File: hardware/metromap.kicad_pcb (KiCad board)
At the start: 4 copper layers, 100 x 100 mm, 138 parts, among them J1 USB_C_Receptacle_USB2.0_16P, U1 AZ1117-3.3, U2 ESP32-C6-MINI-1-H4, U3 SN74LVC1G125DBV

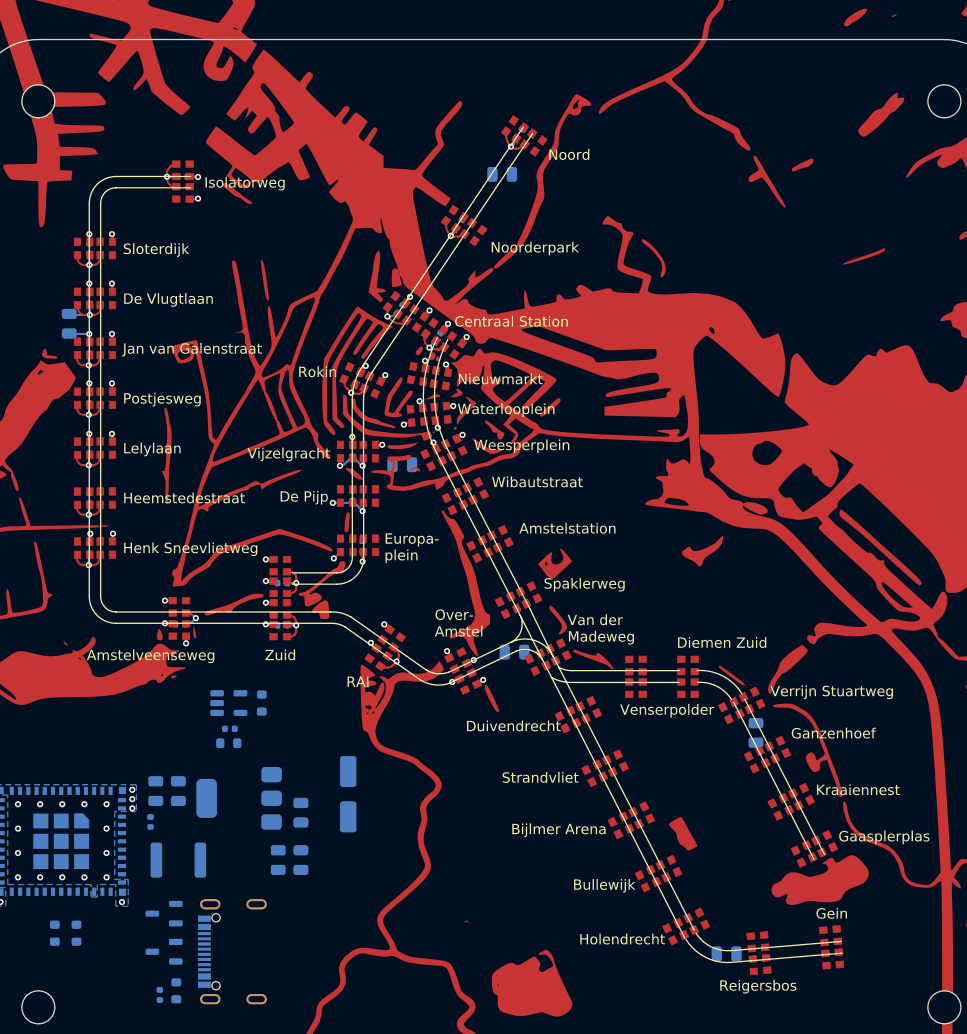
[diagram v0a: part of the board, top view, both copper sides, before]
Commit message: Routed half of leds
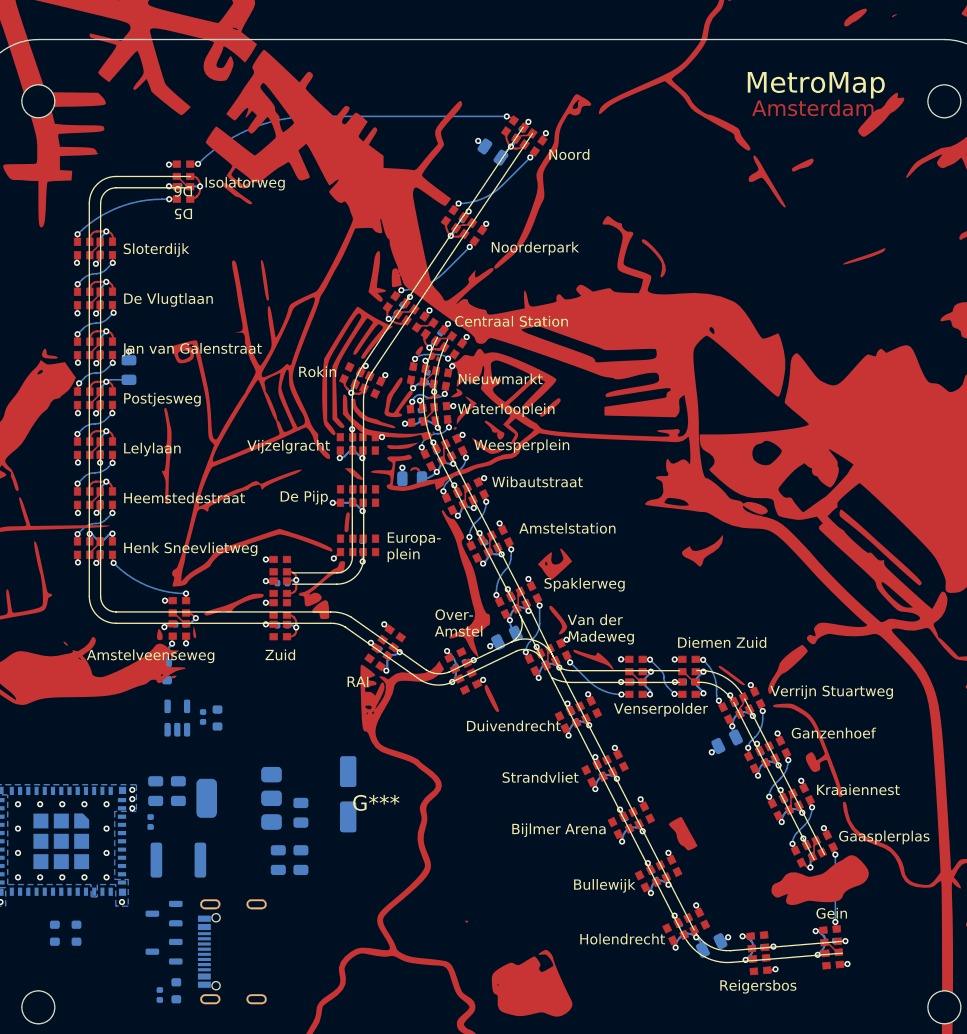
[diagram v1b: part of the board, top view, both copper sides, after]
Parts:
- removed the D3 at (82.2, 41.7)
- removed the D4 at (82.2, 43.9)
- added C35: 100n, Capacitor_SMD:C_0402_1005Metric, B.Cu at (107.1, 69.4)
- added C36: 100n, Capacitor_SMD:C_0402_1005Metric, B.Cu at (109.2, 73.6)
- added C37: 100n, Capacitor_SMD:C_0402_1005Metric, B.Cu at (114.4, 83.7)
- added C38: 100n, Capacitor_SMD:C_0402_1005Metric, B.Cu at (120.2, 94.8)
- added C39: 100n, Capacitor_SMD:C_0402_1005Metric, B.Cu at (122.8, 100.0)
- added C40: 100n, Capacitor_SMD:C_0402_1005Metric, B.Cu at (105.4, 65.5)
- added C41: 100n, Capacitor_SMD:C_0402_1005Metric, B.Cu at (111.8, 78.3)
- added C42: 100n, Capacitor_SMD:C_0402_1005Metric, B.Cu at (101.7, 88.5)
- added C43: 100n, Capacitor_SMD:C_0402_1005Metric, B.Cu at (128.0, 110.2)
- added C44: 100n, Capacitor_SMD:C_0402_1005Metric, B.Cu at (125.4, 105.1)
- added C45: 100n, Capacitor_SMD:C_0402_1005Metric, B.Cu at (105.9, 61.8)
- added C46: 100n, Capacitor_SMD:C_0402_1005Metric, B.Cu at (109.2, 89.7)
- added C47: 100n, Capacitor_SMD:C_0402_1005Metric, B.Cu at (117.2, 89.2)
- added C48: 100n, Capacitor_SMD:C_0402_1005Metric, B.Cu at (130.7, 115.4)
- added C49: 100n, Capacitor_SMD:C_0402_1005Metric, B.Cu at (126.3, 91.4)
- added C50: 100n, Capacitor_SMD:C_0402_1005Metric, B.Cu at (131.4, 91.4)
- added C51: 100n, Capacitor_SMD:C_0402_1005Metric, B.Cu at (136.1, 93.9)
- added C52: 100n, Capacitor_SMD:C_0402_1005Metric, B.Cu at (138.6, 98.7)
- added C53: 100n, Capacitor_SMD:C_0402_1005Metric, B.Cu at (140.9, 103.3)
- added C54: 100n, Capacitor_SMD:C_0402_1005Metric, B.Cu at (143.1, 107.8)
- added C55: 100n, Capacitor_SMD:C_0402_1005Metric, B.Cu at (145.1, 116.6)
- added C56: 100n, Capacitor_SMD:C_0402_1005Metric, B.Cu at (138.1, 117.2)
- added D5: SK6812-EC20, metro-tracker:RGB_LED_2020, F.Cu at (82.3, 43.9)
- added D6: SK6812-EC20, metro-tracker:RGB_LED_2020, F.Cu at (82.3, 41.7)
- moved D42 29.2 mm to (74.8, 49.3), turned to -90 degrees
- moved D10 29.2 mm to (72.6, 78.4), turned to -90 degrees
- moved D9 29.2 mm to (74.8, 78.4), turned to -90 degrees
- moved D43 29.2 mm to (72.6, 49.3), turned to -90 degrees
- moved C26 29.1 mm to (74.2, 49.3), turned to -90 degrees
- moved C18 29.1 mm to (74.2, 78.4), turned to -90 degrees
- moved D38 19.5 mm to (74.8, 54.1), turned to -90 degrees
- moved D21 19.5 mm to (72.6, 73.5), turned to -90 degrees
- moved D20 19.5 mm to (74.8, 73.5), turned to -90 degrees
- moved D39 19.5 mm to (72.6, 54.1), turned to -90 degrees
- moved C27 19.4 mm to (74.2, 54.1), turned to -90 degrees
- moved C19 19.4 mm to (74.2, 73.5), turned to -90 degrees
- moved D73 9.96 mm to (74.8, 59.0), turned to -90 degrees
- moved D26 9.95 mm to (72.6, 68.7), turned to -90 degrees
- moved D25 9.94 mm to (74.8, 68.7), turned to -90 degrees
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- renumbered C34 to C1, C26 to C10, C28 to C11, C29 to C12, C30 to C13, C31 to C14, C25 to C15, C19 to C16, C20 to C17, C21 to C18, C22 to C19, C33 to C2, C23 to C20, C24 to C21, C13 to C22, C14 to C23, C15 to C24, C16 to C25, C17 to C26, C18 to C27, C12 to C28, C11 to C29, C32 to C3, C10 to C30, C9 to C31, C8 to C32, C7 to C33, C6 to C34, C5 to C4, C4 to C5, C3 to C6, C1 to C7, C2 to C8, C27 to C9, D83 to D1, D8 to D10, D9 to D11, D31 to D12, D32 to D13, D79 to D14, D80 to D15, D81 to D16, D82 to D17, D77 to D18, D78 to D19, D84 to D2, D10 to D20, D11 to D21, D12 to D22, D13 to D23, D14 to D24, D15 to D25, D16 to D26, D17 to D27, D18 to D28, D19 to D29, D1 to D3, D20 to D30, D21 to D31, D22 to D32, D23 to D33, D24 to D34, D25 to D35, D26 to D36, D33 to D37, D34 to D38, D35 to D39, D2 to D4, D36 to D40, D37 to D41, D38 to D42, D39 to D43, D40 to D44, D41 to D45, D42 to D46, D43 to D47, D44 to D48, D45 to D49, D46 to D50, D47 to D51, D48 to D52, D49 to D53, D56 to D54, D57 to D55, D58 to D56, D59 to D57, D60 to D58, D61 to D59, D62 to D60, D63 to D61, D64 to D62, D65 to D63, D66 to D64, D67 to D65, D68 to D66, D69 to D67, D70 to D68, D71 to D69, D5 to D7, D72 to D70, D55 to D71, D30 to D72, D28 to D73, D29 to D74, D74 to D75, D75 to D76, D76 to D77, D51 to D78, D52 to D79, D6 to D8, D53 to D80, D73 to D81, D50 to D82, D27 to D83, D54 to D84, D7 to D9, R6 to R1, R7 to R2, R1 to R3, R2 to R4, R3 to R5, R8 to R6, R4 to R7, R5 to R8, U3 to U2, U2 to U3
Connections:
- D10 pad 4: Net-(D8-DOUT) -> Net-(D10-DOUT)
- D11 pad 2: Net-(D8-DOUT) -> Net-(D11-DIN)
- D11 pad 4: Net-(D31-DIN) -> Net-(D11-DOUT)
- D12 pad 2: Net-(D31-DIN) -> Net-(D12-DIN)
- D12 pad 4: Net-(D31-DOUT) (its old number) -> Net-(D12-DOUT)
- D13 pad 2: Net-(D31-DOUT) (its old number) -> unconnected-(D13-DIN-Pad2)
- D13 pad 4: Net-(D32-DOUT) -> unconnected-(D13-DOUT-Pad4)
- D14 pad 2: Net-(D32-DOUT) -> unconnected-(D14-DIN-Pad2)
- D14 pad 4: Net-(D79-DOUT) -> unconnected-(D14-DOUT-Pad4)
- D15 pad 2: Net-(D79-DOUT) -> unconnected-(D15-DIN-Pad2)
- D15 pad 4: Net-(D80-DOUT) -> unconnected-(D15-DOUT-Pad4)
- D16 pad 2: Net-(D80-DOUT) -> Net-(D16-DIN)
- D16 pad 4: Net-(D81-DOUT) -> unconnected-(D16-DOUT-Pad4)
- D17 pad 2: Net-(D81-DOUT) -> unconnected-(D17-DIN-Pad2)
- D17 pad 4: Net-(D77-DIN) -> unconnected-(D17-DOUT-Pad4)
- D18 pad 2: Net-(D77-DIN) -> unconnected-(D18-DIN-Pad2)
- D18 pad 4: Net-(D77-DOUT) -> unconnected-(D18-DOUT-Pad4)
- D19 pad 2: Net-(D77-DOUT) -> Net-(D19-DIN)
- D19 pad 4: Net-(D10-DIN) (its old number) -> Net-(D16-DIN)
- D20 pad 2: Net-(D10-DIN) (its old number) -> Net-(D10-DOUT)
- D21 pad 4: Net-(D11-DOUT) -> Net-(D21-DOUT)
- D24 pad 4: Net-(D14-DOUT) -> Net-(D24-DOUT)
- D25 pad 2: Net-(D14-DOUT) -> Net-(D21-DOUT)
- D26 pad 4: Net-(D16-DOUT) -> Net-(D26-DOUT)
- D27 pad 2: Net-(D16-DOUT) -> Net-(D27-DIN)
- D27 pad 4: Net-(D17-DOUT) -> Net-(D27-DOUT)
- D28 pad 2: Net-(D17-DOUT) -> unconnected-(D28-DIN-Pad2)
- D28 pad 4: Net-(D18-DOUT) -> unconnected-(D28-DOUT-Pad4)
- D29 pad 2: Net-(D18-DOUT) -> Net-(D24-DOUT)
- D29 pad 4: Net-(D19-DOUT) -> Net-(D27-DIN)
- D3 pad 2: /LEDs/DATA_IN -> Net-(D3-DIN)
- D30 pad 2: Net-(D19-DOUT) -> unconnected-(D30-DIN-Pad2)
- D30 pad 4: Net-(D20-DOUT) (its old number) -> unconnected-(D30-DOUT-Pad4)
- D31 pad 2: Net-(D20-DOUT) (its old number) -> Net-(D26-DOUT)
- D32 pad 4: Net-(D22-DOUT) (its old number) -> Net-(D32-DOUT)
- D33 pad 2: Net-(D22-DOUT) (its old number) -> Net-(D33-DIN)
- D33 pad 4: Net-(D23-DOUT) (its old number) -> Net-(D33-DOUT)
- D34 pad 2: Net-(D23-DOUT) (its old number) -> Net-(D27-DOUT)
- D34 pad 4: Net-(D24-DOUT) -> Net-(D33-DIN)
- D35 pad 2: Net-(D24-DOUT) -> Net-(D35-DIN)
- D35 pad 4: Net-(D25-DOUT) (its old number) -> Net-(D35-DOUT)
- D36 pad 2: Net-(D25-DOUT) (its old number) -> unconnected-(D36-DIN-Pad2)
- D36 pad 4: Net-(D26-DOUT) -> unconnected-(D36-DOUT-Pad4)
- D37 pad 2: Net-(D26-DOUT) -> unconnected-(D37-DIN-Pad2)
- D37 pad 4: Net-(D33-DOUT) -> unconnected-(D37-DOUT-Pad4)
- D38 pad 2: Net-(D33-DOUT) -> Net-(D38-DIN)
- D39 pad 4: Net-(D35-DOUT) -> Net-(D39-DOUT)
- D4 pad 4: Net-(D2-DOUT) -> Net-(D4-DOUT)
- D40 pad 4: Net-(D36-DOUT) -> Net-(D12-DIN)
- D41 pad 2: Net-(D36-DOUT) -> Net-(D41-DIN)
- D41 pad 4: Net-(D37-DOUT) -> Net-(D41-DOUT)
- D42 pad 2: Net-(D37-DOUT) -> Net-(D39-DOUT)
- D43 pad 4: Net-(D39-DOUT) -> Net-(D43-DOUT)
- D44 pad 2: Net-(D39-DOUT) -> unconnected-(D44-DIN-Pad2)
- D44 pad 4: Net-(D40-DOUT) -> unconnected-(D44-DOUT-Pad4)
- D45 pad 2: Net-(D40-DOUT) -> unconnected-(D45-DIN-Pad2)
- D45 pad 4: Net-(D41-DOUT) -> unconnected-(D45-DOUT-Pad4)
- D46 pad 2: Net-(D41-DOUT) -> Net-(D12-DOUT)
- D46 pad 4: Net-(D42-DOUT) (its old number) -> Net-(D41-DIN)
- D47 pad 2: Net-(D42-DOUT) (its old number) -> unconnected-(D47-DIN-Pad2)
- D47 pad 4: Net-(D43-DOUT) -> unconnected-(D47-DOUT-Pad4)
- D48 pad 2: Net-(D43-DOUT) -> unconnected-(D48-DIN-Pad2)
- D48 pad 4: Net-(D44-DOUT) -> unconnected-(D48-DOUT-Pad4)
- D49 pad 2: Net-(D44-DOUT) -> Net-(D49-DIN)
- D49 pad 4: Net-(D45-DOUT) -> Net-(D49-DOUT)
- D50 pad 2: Net-(D45-DOUT) -> Net-(D50-DIN)
- D50 pad 4: Net-(D46-DOUT) -> Net-(D50-DOUT)
- D51 pad 2: Net-(D46-DOUT) -> unconnected-(D51-DIN-Pad2)
- D51 pad 4: Net-(D47-DOUT) -> unconnected-(D51-DOUT-Pad4)
- D52 pad 2: Net-(D47-DOUT) -> Net-(D41-DOUT)
- D52 pad 4: Net-(D48-DOUT) -> Net-(D49-DIN)
- D53 pad 2: Net-(D48-DOUT) -> unconnected-(D53-DIN-Pad2)
- D53 pad 4: Net-(D49-DOUT) -> unconnected-(D53-DOUT-Pad4)
- D54 pad 2: Net-(D49-DOUT) -> Net-(D54-DIN)
- D55 pad 4: Net-(D57-DOUT) -> Net-(D55-DOUT)
- D56 pad 2: Net-(D57-DOUT) -> unconnected-(D56-DIN-Pad2)
- D56 pad 4: Net-(D58-DOUT) -> unconnected-(D56-DOUT-Pad4)
- D57 pad 2: Net-(D58-DOUT) -> Net-(D57-DIN)
- D57 pad 4: Net-(D59-DOUT) -> Net-(D54-DIN)
- D58 pad 2: Net-(D59-DOUT) -> Net-(D55-DOUT)
- D58 pad 4: Net-(D60-DOUT) -> Net-(D58-DOUT)
- D59 pad 2: Net-(D60-DOUT) -> Net-(D59-DIN)
- D59 pad 4: Net-(D61-DOUT) -> Net-(D59-DOUT)
- D60 pad 2: Net-(D61-DOUT) -> unconnected-(D60-DIN-Pad2)
- D60 pad 4: Net-(D62-DOUT) -> unconnected-(D60-DOUT-Pad4)
- D61 pad 2: Net-(D62-DOUT) -> Net-(D58-DOUT)
- D61 pad 4: Net-(D63-DOUT) -> Net-(D59-DIN)
- D62 pad 2: Net-(D63-DOUT) -> unconnected-(D62-DIN-Pad2)
- D62 pad 4: Net-(D64-DOUT) -> unconnected-(D62-DOUT-Pad4)
- D63 pad 2: Net-(D64-DOUT) -> Net-(D63-DIN)
- D63 pad 4: Net-(D65-DOUT) -> Net-(D63-DOUT)
- D64 pad 2: Net-(D65-DOUT) -> Net-(D59-DOUT)
- D64 pad 4: Net-(D66-DOUT) -> Net-(D63-DIN)
- D65 pad 2: Net-(D66-DOUT) -> unconnected-(D65-DIN-Pad2)
- D65 pad 4: Net-(D67-DOUT) -> unconnected-(D65-DOUT-Pad4)
- D66 pad 2: Net-(D67-DOUT) -> unconnected-(D66-DIN-Pad2)
- D66 pad 4: Net-(D68-DOUT) -> unconnected-(D66-DOUT-Pad4)
- D67 pad 2: Net-(D68-DOUT) -> Net-(D67-DIN)
- D67 pad 4: Net-(D69-DOUT) -> Net-(D67-DOUT)
- D68 pad 2: Net-(D69-DOUT) -> Net-(D63-DOUT)
- D68 pad 4: Net-(D70-DOUT) -> Net-(D67-DIN)
- D69 pad 2: Net-(D70-DOUT) -> unconnected-(D69-DIN-Pad2)
- D69 pad 4: Net-(D71-DOUT) -> unconnected-(D69-DOUT-Pad4)
- D70 pad 2: Net-(D71-DOUT) -> unconnected-(D70-DIN-Pad2)
- D70 pad 4: Net-(D55-DIN) -> unconnected-(D70-DOUT-Pad4)
- D71 pad 2: Net-(D55-DIN) -> Net-(D49-DOUT)
- D71 pad 4: Net-(D30-DIN) -> Net-(D71-DOUT)
- D72 pad 2: Net-(D30-DIN) -> Net-(D33-DOUT)
- D72 pad 4: Net-(D28-DIN) -> Net-(D35-DIN)
- D73 pad 2: Net-(D28-DIN) -> Net-(D32-DOUT)
- D74 pad 4: Net-(D29-DOUT) -> Net-(D38-DIN)
- D75 pad 2: Net-(D29-DOUT) -> Net-(D67-DOUT)
- D75 pad 4: Net-(D74-DOUT) -> Net-(D75-DOUT)
- D76 pad 2: Net-(D74-DOUT) -> unconnected-(D76-DIN-Pad2)
- D76 pad 4: Net-(D75-DOUT) -> unconnected-(D76-DOUT-Pad4)
- D77 pad 2: Net-(D75-DOUT) -> unconnected-(D77-DIN-Pad2)
- D77 pad 4: Net-(D51-DIN) -> unconnected-(D77-DOUT-Pad4)
- D78 pad 2: Net-(D51-DIN) -> unconnected-(D78-DIN-Pad2)
- D78 pad 4: Net-(D51-DOUT) -> unconnected-(D78-DOUT-Pad4)
- D79 pad 2: Net-(D51-DOUT) -> Net-(D71-DOUT)
- D79 pad 4: Net-(D52-DOUT) -> Net-(D57-DIN)
- D8 pad 4: Net-(D6-DOUT) -> Net-(D11-DIN)
- D80 pad 2: Net-(D52-DOUT) -> unconnected-(D80-DIN-Pad2)
- D80 pad 4: Net-(D53-DOUT) -> unconnected-(D80-DOUT-Pad4)
- D81 pad 2: Net-(D53-DOUT) -> Net-(D75-DOUT)
- D81 pad 4: Net-(D50-DIN) -> Net-(D19-DIN)
- D82 pad 2: Net-(D50-DIN) -> /LEDs/DATA_IN
- D82 pad 4: Net-(D27-DIN) -> Net-(D50-DIN)
- D83 pad 2: Net-(D27-DIN) -> unconnected-(D83-DIN-Pad2)
- D83 pad 4: Net-(D27-DOUT) -> unconnected-(D83-DOUT-Pad4)
- D84 pad 2: Net-(D27-DOUT) -> unconnected-(D84-DIN-Pad2)
- D9 pad 2: Net-(D6-DOUT) -> Net-(D50-DOUT)
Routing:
- net +5V: track 91.6 -> 187.8 mm, vias 30 -> 67
- net GND: track 44.0 -> 104.8 mm, vias 58 -> 106
- net Net-(D3-DIN): track 0.00 -> 32.7 mm, vias 0 -> 2
- net Net-(D43-DOUT): track 0.00 -> 11.2 mm, vias 0 -> 2
- net Net-(D4-DOUT): track 0.00 -> 10.1 mm, vias 0 -> 2
- net Net-(D11-DIN): track 0.00 -> 9.67 mm, vias 0 -> 2
- net Net-(D50-DOUT): track 0.00 -> 9.31 mm, vias 0 -> 2
- net Net-(D19-DIN): track 0.00 -> 8.04 mm, vias 0 -> 2
- net Net-(D57-DIN): track 0.00 -> 7.73 mm, vias 0 -> 2
- net Net-(D49-DOUT): track 0.00 -> 6.44 mm, vias 0 -> 2
- net Net-(D41-DOUT): track 0.00 -> 6.34 mm, vias 0 -> 2
- net Net-(D58-DOUT): track 0.00 -> 5.89 mm, vias 0 -> 2
- net Net-(D38-DIN): track 0.00 -> 5.71 mm, vias 0 -> 2
- net Net-(D54-DOUT): track 0.00 -> 5.70 mm, vias 0 -> 2
- net Net-(D67-DOUT): track 0.00 -> 5.64 mm, vias 0 -> 2
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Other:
- board text added: "Amsterdam"
- board text added: "BRS 2026"
- board text added: "MetroMap"
